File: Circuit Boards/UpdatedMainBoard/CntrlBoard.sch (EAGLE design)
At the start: 45 parts, among them P1 22-23-2021, P10 3PIN2MMPITCH, P11 3PIN2MMPITCH, P12 DF3A-2P-2DSA, P13 DF3A-2P-2DSA, P14 DF3A-2P-2DSA, P15 DF3A-2P-2DSA, P16 DF3A-2P-2DSA, P17 DF3A-2P-2DSA, P2 22-23-2021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

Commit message: Control Board update finished
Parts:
- added P18, P19, P20, P21: DF3A-2P-2DSA, con-3m:DF3A-2P-2DSA
- added R13: 100R, resistor:R-US_R1206
- added R14: 300R, resistor:R-US_R1206
- added U$3: RSHUNT, resistor:RSHUNT
- added U$4: LT6106, linear-technology:LT6106
- P10, P11, P7, P8, P9: value 3PIN2MMPITCH -> 3MM2MMLOCKING; device con-3m:3PIN2MMPITCH -> con-3m:3MM2MMLOCKING
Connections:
- new net N$22: SW1.O, U$3.I2
- new net N$24: R13.1, U$3.E2
- new net N$25: R13.2, U$4.-IN
- new net N$26: U$3.E1, U$4.+IN
- new net RX1: P18G$1.KL, U1.19(RX1)
- new net RX2: P19G$1.KL, U1.17(RX2)
- new net SCL: P20G$1.KL, U1.21(SCL)
- new net SDA: P20G$2.KL, U1.20(SDA)
- new net TX1: P18G$2.KL, U1.18(TX1)
- new net TX2: P19G$2.KL, U1.16(TX2)
- new net V_CURRENT: R14.1, U$4.OUT, U1.A7
- net AIN1: now also U1.28; no longer U1.26
- net AIN2: now also U1.26; no longer U1.28
- net GND: now also R14.2, U$4.V-
- net PUMP_DIR_RELAY: now also P21G$1.KL
- net VCC: now also U$3.I1, U$4.V+; no longer SW1.O
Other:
- note added: "SPARE SERIAL"
- moved on the sheet: SW1

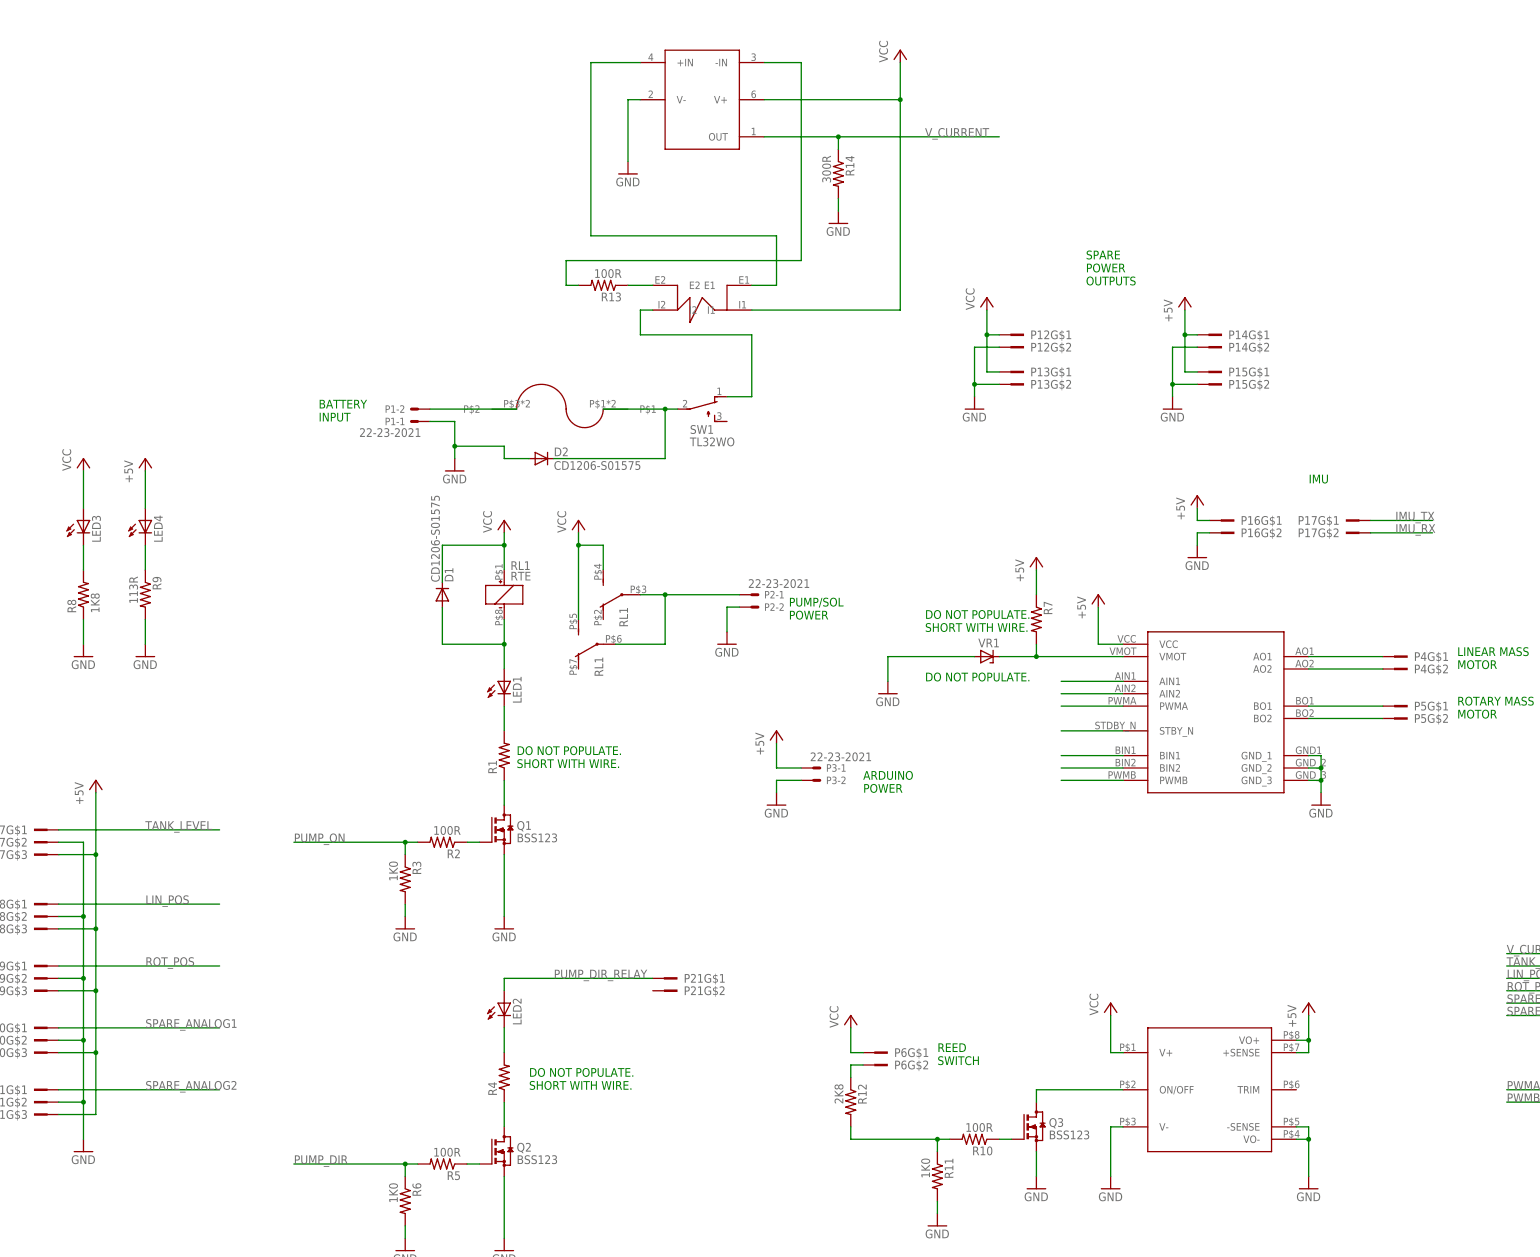
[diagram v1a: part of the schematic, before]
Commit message: Added 6 pin connector
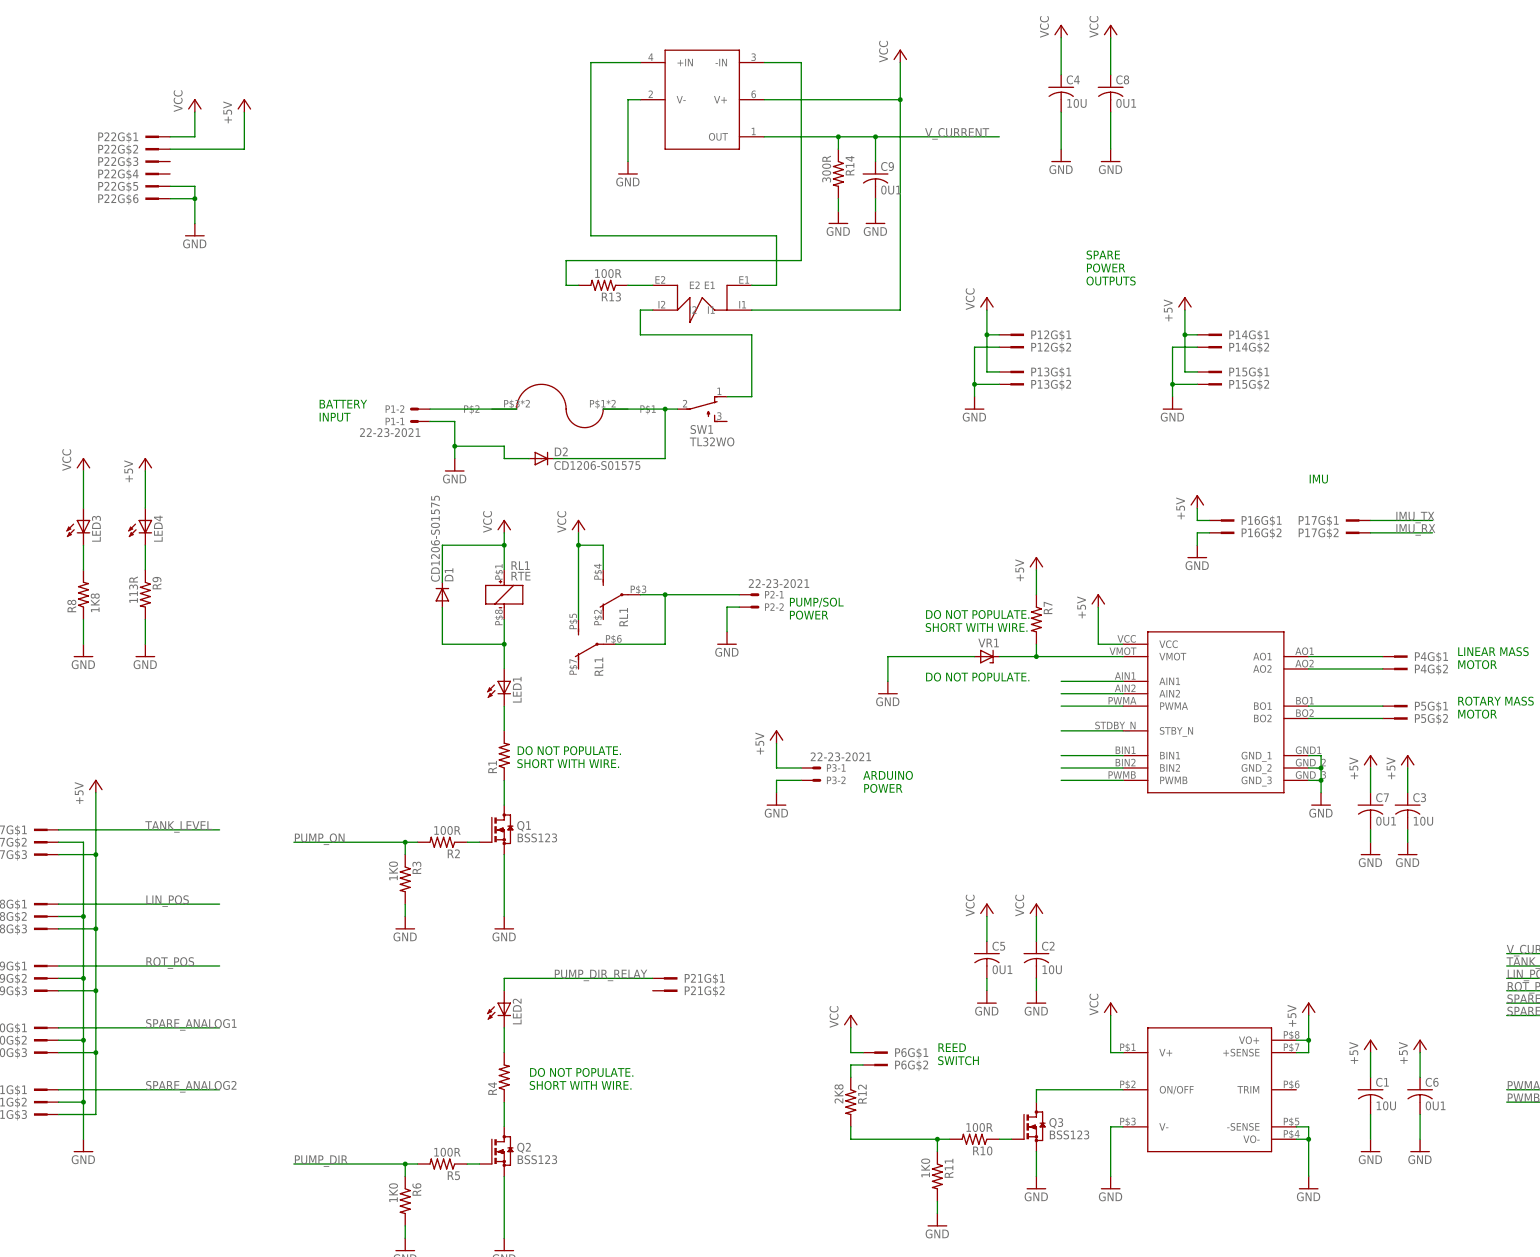
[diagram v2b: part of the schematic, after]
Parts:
- added C1, C2, C3, C4: 10U, resistor:C-USC1210K
- added C5, C6, C7, C8, C9: 0U1, resistor:C-USC1210K
- added P22: 6PIN2ROWARDUINO, con-3m:6PIN2ROWARDUINO
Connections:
- net +5V: now also C1.1, C3.1, C6.1, C7.1, P22G$2.KL
- net GND: now also C1.2, C2.2, C3.2, C4.2, C5.2, C6.2, C7.2, C8.2, C9.2, P22G$5.KL, P22G$6.KL
- net VCC: now also C2.1, C4.1, C5.1, C8.1, P22G$1.KL
- net V_CURRENT: now also C9.1
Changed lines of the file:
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@@
 <part name="R14" library="resistor" deviceset="R-US_" device="R1206" value="300R"/>
 <part name="GND22" library="supply1" deviceset="GND" device=""/>
+<part name="C1" library="resistor" deviceset="C-US" device="C1210K" value="10U"/>
+<part name="C2" library="resistor" deviceset="C-US" device="C1210K" value="10U"/>
+<part name="C3" library="resistor" deviceset="C-US" device="C1210K" value="10U"/>
+<part name="C4" library="resistor" deviceset="C-US" device="C1210K" value="10U"/>
+<part name="C5" library="resistor" deviceset="C-US" device="C1210K" value="0U1"/>
+<part name="C6" library="resistor" deviceset="C-US" device="C1210K" value="0U1"/>
+<part name="C7" library="resistor" deviceset="C-US" device="C1210K" value="0U1"/>
+<part name="C8" library="resistor" deviceset="C-US" device="C1210K" value="0U1"/>
+<part name="C9" library="resistor" deviceset="C-US" device="C1210K" value="0U1"/>
+<part name="GND23" library="supply1" deviceset="GND" device=""/>
+<part name="GND24" library="supply1" deviceset="GND" device=""/>
+<part name="GND25" library="supply1" deviceset="GND" device=""/>
+<part name="P+17" library="supply1" deviceset="VCC" device=""/>
+<part name="P+18" library="supply1" deviceset="VCC" device=""/>
+<part name="P+19" library="supply1" deviceset="+5V" device=""/>
+<part name="P+20" library="supply1" deviceset="+5V" device=""/>
+<part name="GND26" library="supply1" deviceset="GND" device=""/>
+<part name="GND27" library="supply1" deviceset="GND" device=""/>
+<part name="P+21" library="supply1" deviceset="+5V" device=""/>
+<part name="P+22" library="supply1" deviceset="+5V" device=""/>
+<part name="P+23" library="supply1" deviceset="VCC" device=""/>
+<part name="P+24" library="supply1" deviceset="VCC" device=""/>
+<part name="GND28" library="supply1" deviceset="GND" device=""/>
+<part name="GND29" library="supply1" deviceset="GND" device=""/>
+<part name="GND30" library="supply1" deviceset="GND" device=""/>
+<part name="GND31" library="supply1" deviceset="GND" device=""/>
+<part name="P22" library="con-3m" deviceset="6PIN2ROWARDUINO" device=""/>
+<part name="P+25" library="supply1" deviceset="VCC" device=""/>
+<part name="GND32" library="supply1" deviceset="GND" device=""/>
+<part name="P+26" library="supply1" deviceset="+5V" device=""/>
 </parts>
 <sheets>
@@
 <instance part="R14" gate="G$1" x="30.48" y="144.78" rot="R270"/>
 <instance part="GND22" gate="1" x="30.48" y="134.62"/>
+<instance part="C1" gate="G$1" x="139.7" y="-43.18"/>
+<instance part="C2" gate="G$1" x="71.12" y="-15.24"/>
+<instance part="C3" gate="G$1" x="147.32" y="15.24"/>
+<instance part="C4" gate="G$1" x="76.2" y="162.56"/>
+<instance part="C5" gate="G$1" x="60.96" y="-15.24"/>
+<instance part="C6" gate="G$1" x="149.86" y="-43.18"/>
+<instance part="C7" gate="G$1" x="139.7" y="15.24"/>
+<instance part="C8" gate="G$1" x="86.36" y="162.56"/>
+<instance part="C9" gate="G$1" x="38.1" y="144.78"/>
+<instance part="GND23" gate="1" x="38.1" y="134.62"/>
+<instance part="GND24" gate="1" x="76.2" y="147.32"/>
+<instance part="GND25" gate="1" x="86.36" y="147.32"/>
+<instance part="P+17" gate="VCC" x="76.2" y="175.26"/>
+<instance part="P+18" gate="VCC" x="86.36" y="175.26"/>
+<instance part="P+19" gate="1" x="147.32" y="25.4"/>
+<instance part="P+20" gate="1" x="139.7" y="25.4"/>
+<instance part="GND26" gate="1" x="139.7" y="5.08"/>
+<instance part="GND27" gate="1" x="147.32" y="5.08"/>
+<instance part="P+21" gate="1" x="149.86" y="-33.02"/>
+<instance part="P+22" gate="1" x="139.7" y="-33.02"/>
+<instance part="P+23" gate="VCC" x="71.12" y="-5.08"/>
+<instance part="P+24" gate="VCC" x="60.96" y="-5.08"/>
+<instance part="GND28" gate="1" x="60.96" y="-25.4"/>
+<instance part="GND29" gate="1" x="71.12" y="-25.4"/>
+<instance part="GND30" gate="1" x="139.7" y="-55.88"/>
+<instance part="GND31" gate="1" x="149.86" y="-55.88"/>
+<instance part="P22" gate="G$1" x="-111.76" y="152.4"/>
+<instance part="P22" gate="G$2" x="-111.76" y="149.86"/>
+<instance part="P22" gate="G$3" x="-111.76" y="147.32"/>
+<instance part="P22" gate="G$4" x="-111.76" y="144.78"/>
+<instance part="P22" gate="G$5" x="-111.76" y="142.24"/>
+<instance part="P22" gate="G$6" x="-111.76" y="139.7"/>
+<instance part="P+25" gate="VCC" x="-101.6" y="160.02"/>
+<instance part="GND32" gate="1" x="-101.6" y="132.08"/>
+<instance part="P+26" gate="1" x="-91.44" y="160.02"/>
 </instances>
 <busses>
@@
 <wire x1="30.48" y1="137.16" x2="30.48" y2="139.7" width="0.1524" layer="91"/>
 </segment>
+<segment>
+<pinref part="GND24" gate="1" pin="GND"/>
+<pinref part="C4" gate="G$1" pin="2"/>
+<wire x1="76.2" y1="149.86" x2="76.2" y2="157.48" width="0.1524" layer="91"/>
+</segment>
+<segment>
+<pinref part="GND25" gate="1" pin="GND"/>
+<pinref part="C8" gate="G$1" pin="2"/>
+<wire x1="86.36" y1="149.86" x2="86.36" y2="157.48" width="0.1524" layer="91"/>
+</segment>
+<segment>
+<pinref part="C9" gate="G$1" pin="2"/>
+<pinref part="GND23" gate="1" pin="GND"/>
+<wire x1="38.1" y1="139.7" x2="38.1" y2="137.16" width="0.1524" layer="91"/>
+</segment>
+<segment>
+<pinref part="C3" gate="G$1" pin="2"/>
+<pinref part="GND27" gate="1" pin="GND"/>
+<wire x1="147.32" y1="10.16" x2="147.32" y2="7.62" width="0.1524" layer="91"/>
+</segment>
+<segment>
+<pinref part="GND26" gate="1" pin="GND"/>
+<pinref part="C7" gate="G$1" pin="2"/>
+<wire x1="139.7" y1="7.62" x2="139.7" y2="10.16" width="0.1524" layer="91"/>
+</segment>
+<segment>
+<pinref part="GND29" gate="1" pin="GND"/>
+<pinref part="C2" gate="G$1" pin="2"/>
+<wire x1="71.12" y1="-22.86" x2="71.12" y2="-20.32" width="0.1524" layer="91"/>
+</segment>
+<segment>
+<pinref part="GND28" gate="1" pin="GND"/>
+<pinref part="C5" gate="G$1" pin="2"/>
+<wire x1="60.96" y1="-22.86" x2="60.96" y2="-20.32" width="0.1524" layer="91"/>
+</segment>
+<segment>
+<pinref part="C1" gate="G$1" pin="2"/>
+<pinref part="GND30" gate="1" pin="GND"/>
+<wire x1="139.7" y1="-48.26" x2="139.7" y2="-53.34" width="0.1524" layer="91"/>
+</segment>
+<segment>
+<pinref part="GND31" gate="1" pin="GND"/>
+<pinref part="C6" gate="G$1" pin="2"/>
+<wire x1="149.86" y1="-53.34" x2="149.86" y2="-48.26" width="0.1524" layer="91"/>
+</segment>
+<segment>
+<pinref part="P22" gate="G$6" pin="KL"/>
+<pinref part="GND32" gate="1" pin="GND"/>
+<wire x1="-106.68" y1="139.7" x2="-101.6" y2="139.7" width="0.1524" layer="91"/>
+<wire x1="-101.6" y1="139.7" x2="-101.6" y2="134.62" width="0.1524" layer="91"/>
+<pinref part="P22" gate="G$5" pin="KL"/>
+<wire x1="-106.68" y1="142.24" x2="-101.6" y2="142.24" width="0.1524" layer="91"/>
+<wire x1="-101.6" y1="142.24" x2="-101.6" y2="139.7" width="0.1524" layer="91"/>
+<junction x="-101.6" y="139.7"/>
+</segment>
 </net>
 <net name="N$1" class="0">
@@
 <wire x1="15.24" y1="160.02" x2="43.18" y2="160.02" width="0.1524" layer="91"/>
 <junction x="43.18" y="160.02"/>
+</segment>
+<segment>
+<pinref part="C4" gate="G$1" pin="1"/>
+<pinref part="P+17" gate="VCC" pin="VCC"/>
+<wire x1="76.2" y1="165.1" x2="76.2" y2="172.72" width="0.1524" layer="91"/>
+</segment>
+<segment>
+<pinref part="P+18" gate="VCC" pin="VCC"/>
+<pinref part="C8" gate="G$1" pin="1"/>
+<wire x1="86.36" y1="172.72" x2="86.36" y2="165.1" width="0.1524" layer="91"/>
+</segment>
+<segment>
+<pinref part="C5" gate="G$1" pin="1"/>
+<pinref part="P+24" gate="VCC" pin="VCC"/>
+<wire x1="60.96" y1="-12.7" x2="60.96" y2="-7.62" width="0.1524" layer="91"/>
+</segment>
+<segment>
+<pinref part="C2" gate="G$1" pin="1"/>
+<pinref part="P+23" gate="VCC" pin="VCC"/>
+<wire x1="71.12" y1="-12.7" x2="71.12" y2="-7.62" width="0.1524" layer="91"/>
+</segment>
+<segment>
+<pinref part="P22" gate="G$1" pin="KL"/>
+<pinref part="P+25" gate="VCC" pin="VCC"/>
+<wire x1="-106.68" y1="152.4" x2="-101.6" y2="152.4" width="0.1524" layer="91"/>
+<wire x1="-101.6" y1="152.4" x2="-101.6" y2="157.48" width="0.1524" layer="91"/>
 </segment>
 </net>
@@
 <wire x1="180.34" y1="7.62" x2="180.34" y2="12.7" width="0.1524" layer="91"/>
 </segment>
+<segment>
+<pinref part="P+20" gate="1" pin="+5V"/>
+<pinref part="C7" gate="G$1" pin="1"/>
+<wire x1="139.7" y1="22.86" x2="139.7" y2="17.78" width="0.1524" layer="91"/>
+</segment>
+<segment>
+<pinref part="C3" gate="G$1" pin="1"/>
+<pinref part="P+19" gate="1" pin="+5V"/>
+<wire x1="147.32" y1="17.78" x2="147.32" y2="22.86" width="0.1524" layer="91"/>
+</segment>
+<segment>
+<pinref part="C1" gate="G$1" pin="1"/>
+<pinref part="P+22" gate="1" pin="+5V"/>
+<wire x1="139.7" y1="-40.64" x2="139.7" y2="-35.56" width="0.1524" layer="91"/>
+</segment>
+<segment>
+<pinref part="C6" gate="G$1" pin="1"/>
+<pinref part="P+21" gate="1" pin="+5V"/>
+<wire x1="149.86" y1="-40.64" x2="149.86" y2="-35.56" width="0.1524" layer="91"/>
+</segment>
+<segment>
+<pinref part="P22" gate="G$2" pin="KL"/>
+<pinref part="P+26" gate="1" pin="+5V"/>
+<wire x1="-106.68" y1="149.86" x2="-91.44" y2="149.86" width="0.1524" layer="91"/>
+<wire x1="-91.44" y1="149.86" x2="-91.44" y2="157.48" width="0.1524" layer="91"/>
+</segment>
 </net>
 <net name="N$12" class="0">
@@
 <pinref part="U$4" gate="G$1" pin="OUT"/>
 <wire x1="30.48" y1="152.4" x2="15.24" y2="152.4" width="0.1524" layer="91"/>
-<wire x1="30.48" y1="152.4" x2="63.5" y2="152.4" width="0.1524" layer="91"/>
+<wire x1="30.48" y1="152.4" x2="38.1" y2="152.4" width="0.1524" layer="91"/>
 <junction x="30.48" y="152.4"/>
 <label x="48.26" y="152.4" size="1.778" layer="95"/>
-</segment>
-<segment>
+<pinref part="C9" gate="G$1" pin="1"/>
+<wire x1="38.1" y1="152.4" x2="63.5" y2="152.4" width="0.1524" layer="91"/>
+<wire x1="38.1" y1="147.32" x2="38.1" y2="152.4" width="0.1524" layer="91"/>
+<junction x="38.1" y="152.4"/>
+</segment>
+<segment>
